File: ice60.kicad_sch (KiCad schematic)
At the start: 31 parts, among them J1 SWD, J2 JST SH 4-pin, SW0 SW_Push, U1 RP2040, U2 W25Q128JVS, U3 XC6206PxxxMR, U4 SRV05-4, Y1 12MHz

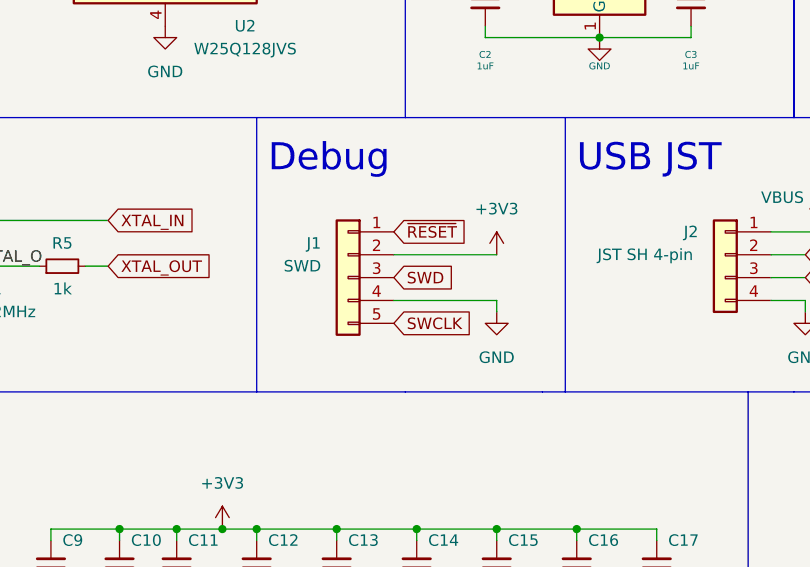
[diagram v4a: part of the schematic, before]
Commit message: swap bulk cap & reroute debug
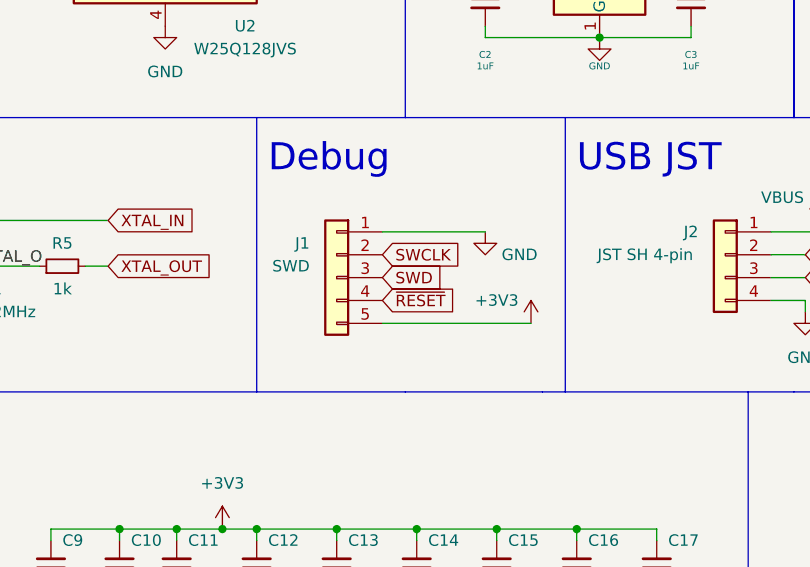
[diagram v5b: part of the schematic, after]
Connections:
- net +3V3: now also J1.5 (Pin_5); no longer J1.2 (Pin_2)
- net GND: now also J1.1 (Pin_1); no longer J1.4 (Pin_4)
- net SWCLK: now also J1.2 (Pin_2); no longer J1.5 (Pin_5)
- net ~{RESET}: now also J1.4 (Pin_4); no longer J1.1 (Pin_1)
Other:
- moved on the sheet: J1
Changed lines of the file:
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@@
     (stroke (width 0) (type default) (color 0 0 0 0))
   )
-  (wire (pts (xy 172.72 74.93) (xy 184.15 74.93))
+  (wire (pts (xy 171.45 67.31) (xy 182.88 67.31))
     (stroke (width 0) (type default) (color 0 0 0 0))
   )
@@
     (stroke (width 0) (type default) (color 0 0 0 0))
   )
-  (wire (pts (xy 184.15 76.2) (xy 184.15 74.93))
-    (stroke (width 0) (type default) (color 0 0 0 0))
-  )
-  (wire (pts (xy 172.72 69.85) (xy 184.15 69.85))
+  (wire (pts (xy 171.45 77.47) (xy 187.96 77.47))
     (stroke (width 0) (type default) (color 0 0 0 0))
   )
@@
     )
   )
-  (global_label "~{RESET}" (shape input) (at 172.72 67.31 0) (fields_autoplaced)
-    (effects (font (size 1.27 1.27)) (justify left))
-    (property "Intersheet References" "${INTERSHEET_REFS}" (id 0) (at 180.8783 67.2306 0)
+  (global_label "~{RESET}" (shape input) (at 171.45 74.93 0) (fields_autoplaced)
+    (effects (font (size 1.27 1.27)) (justify left))
+    (property "Intersheet References" "${INTERSHEET_REFS}" (id 0) (at 179.6083 74.8506 0)
       (effects (font (size 1.27 1.27)) (justify left) hide)
     )
@@
     )
   )
-  (global_label "SWCLK" (shape input) (at 172.72 77.47 0) (fields_autoplaced)
-    (effects (font (size 1.27 1.27)) (justify left))
-    (property "Intersheet References" "${INTERSHEET_REFS}" (id 0) (at 181.3621 77.3906 0)
+  (global_label "SWCLK" (shape input) (at 171.45 69.85 0) (fields_autoplaced)
+    (effects (font (size 1.27 1.27)) (justify left))
+    (property "Intersheet References" "${INTERSHEET_REFS}" (id 0) (at 180.0921 69.7706 0)
       (effects (font (size 1.27 1.27)) (justify left) hide)
     )
@@
     )
   )
-  (global_label "SWD" (shape input) (at 172.72 72.39 0) (fields_autoplaced)
-    (effects (font (size 1.27 1.27)) (justify left))
-    (property "Intersheet References" "${INTERSHEET_REFS}" (id 0) (at 179.0641 72.3106 0)
+  (global_label "SWD" (shape input) (at 171.45 72.39 0) (fields_autoplaced)
+    (effects (font (size 1.27 1.27)) (justify left))
+    (property "Intersheet References" "${INTERSHEET_REFS}" (id 0) (at 177.7941 72.3106 0)
       (effects (font (size 1.27 1.27)) (justify left) hide)
     )
@@
     (pin "2")
   )
-  (symbol (lib_id "power:+3V3") (at 184.15 69.85 0) (unit 1)
-    (in_bom yes) (on_board yes) (fields_autoplaced)
-    (property "Reference" "#PWR021" (id 0) (at 184.15 73.66 0)
-      (effects (font (size 1.27 1.27)) hide)
-    )
-    (property "Value" "+3V3" (id 1) (at 184.15 64.77 0))
-    (property "Footprint" "" (id 2) (at 184.15 69.85 0)
-      (effects (font (size 1.27 1.27)) hide)
-    )
-    (property "Datasheet" "" (id 3) (at 184.15 69.85 0)
+  (symbol (lib_id "power:+3V3") (at 187.96 77.47 0) (unit 1)
+    (in_bom yes) (on_board yes)
+    (property "Reference" "#PWR021" (id 0) (at 187.96 81.28 0)
+      (effects (font (size 1.27 1.27)) hide)
+    )
+    (property "Value" "+3V3" (id 1) (at 184.15 74.93 0))
+    (property "Footprint" "" (id 2) (at 187.96 77.47 0)
+      (effects (font (size 1.27 1.27)) hide)
+    )
+    (property "Datasheet" "" (id 3) (at 187.96 77.47 0)
       (effects (font (size 1.27 1.27)) hide)
     )
@@
     (pin "2")
   )
-  (symbol (lib_id "Connector_Generic:Conn_01x05") (at 167.64 72.39 0) (mirror y) (unit 1)
+  (symbol (lib_id "Connector_Generic:Conn_01x05") (at 166.37 72.39 0) (mirror y) (unit 1)
     (in_bom no) (on_board yes)
-    (property "Reference" "J1" (id 0) (at 163.83 68.58 0))
-    (property "Value" "SWD" (id 1) (at 162.56 71.12 0))
-    (property "Footprint" "Connector_PinSocket_2.54mm:PinSocket_1x05_P2.54mm_Vertical" (id 2) (at 167.64 72.39 0)
-      (effects (font (size 1.27 1.27)) hide)
-    )
-    (property "Datasheet" "~" (id 3) (at 167.64 72.39 0)
+    (property "Reference" "J1" (id 0) (at 162.56 68.58 0))
+    (property "Value" "SWD" (id 1) (at 161.29 71.12 0))
+    (property "Footprint" "Connector_PinSocket_2.54mm:PinSocket_1x05_P2.54mm_Vertical" (id 2) (at 166.37 72.39 0)
+      (effects (font (size 1.27 1.27)) hide)
+    )
+    (property "Datasheet" "~" (id 3) (at 166.37 72.39 0)
       (effects (font (size 1.27 1.27)) hide)
     )
@@
     (pin "1")
   )
-  (symbol (lib_id "power:GND") (at 184.15 76.2 0) (unit 1)
-    (in_bom yes) (on_board yes) (fields_autoplaced)
-    (property "Reference" "#PWR022" (id 0) (at 184.15 82.55 0)
-      (effects (font (size 1.27 1.27)) hide)
-    )
-    (property "Value" "GND" (id 1) (at 184.15 81.28 0))
-    (property "Footprint" "" (id 2) (at 184.15 76.2 0)
-      (effects (font (size 1.27 1.27)) hide)
-    )
-    (property "Datasheet" "" (id 3) (at 184.15 76.2 0)
-      (effects (font (size 1.27 1.27)) hide)
-    )
+  (symbol (lib_id "power:GND") (at 182.88 67.31 0) (unit 1)
+    (in_bom yes) (on_board yes)
+    (property "Reference" "#PWR022" (id 0) (at 182.88 73.66 0)
+      (effects (font (size 1.27 1.27)) hide)
+    )
+    (property "Value" "GND" (id 1) (at 186.69 69.85 0))
+    (property "Footprint" "" (id 2) (at 182.88 67.31 0)
+      (effects (font (size 1.27 1.27)) hide)
+    )
+    (property "Datasheet" "" (id 3) (at 182.88 67.31 0)
+      (effects (font (size 1.27 1.27)) hide)
+    )

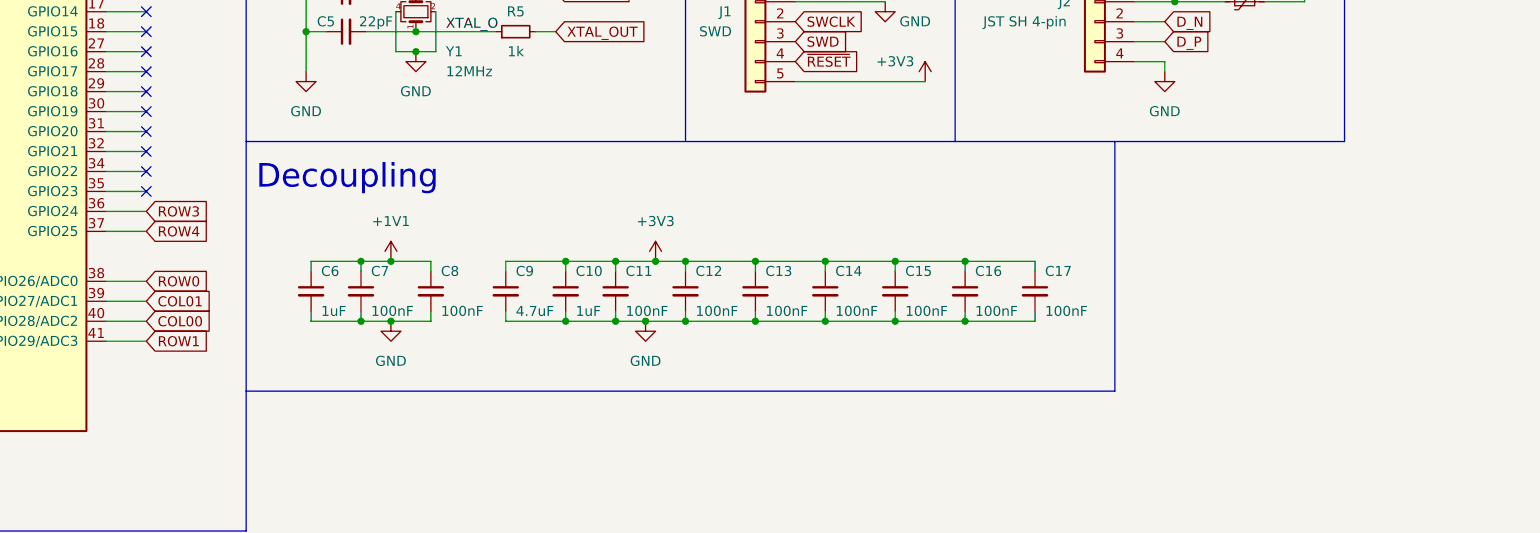
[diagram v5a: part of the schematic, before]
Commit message: add capslock in-switch LED indicator
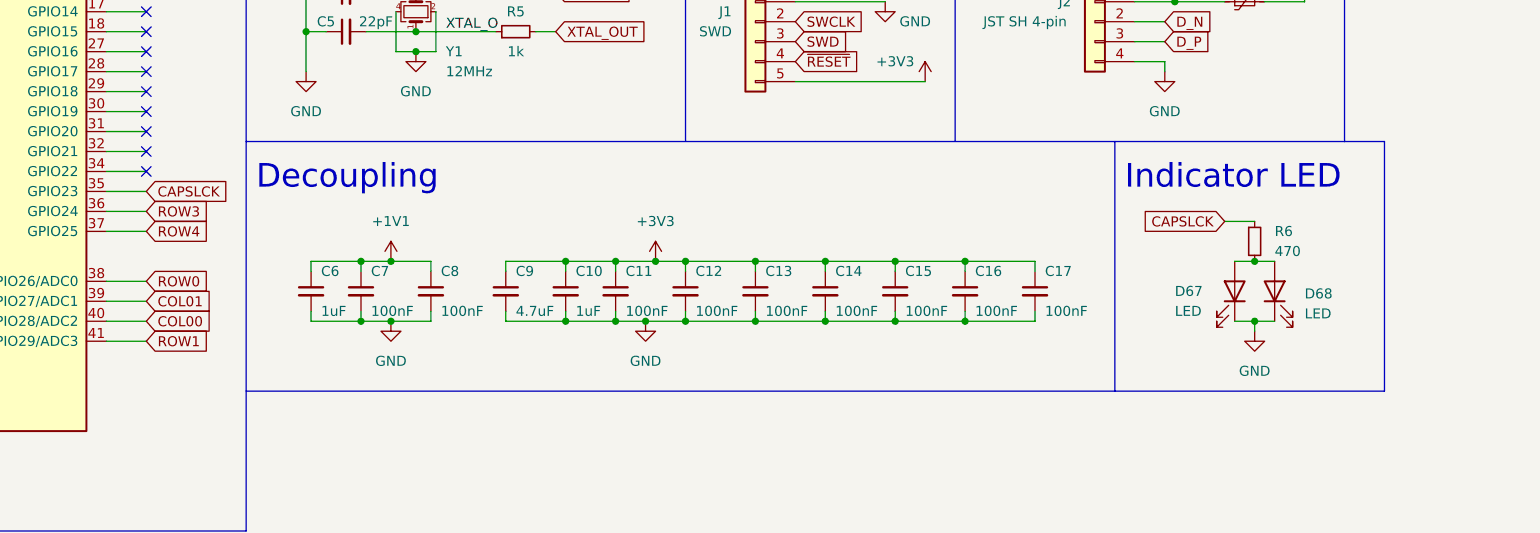
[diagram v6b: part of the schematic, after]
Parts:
- added D67: LED, marbastlib-mx:LED_MX_3mm, symbol Device:LED
- added D68: LED, marbastlib-mx:LED_MX_3mm-FLIPPED, symbol Device:LED
- added R6: 470, Resistor_SMD:R_0402_1005Metric, symbol Device:R_Small
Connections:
- net GND: now also D67.1 (K), D68.1 (K)
- net CAPSLCK: now reaches U1.35 (GPIO23)
- net CAPSLCK: now also R6.1
- new net: D67.2 (A), D68.2 (A), R6.2
- no-connect marks 13 -> 12
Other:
- note added: "Indicator LED"
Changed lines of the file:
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@@
     (comment 4 "60% Soldered PCB with JST Powered by RP2040")
   )
+  (junction (at 229.87 100.33) (diameter 0) (color 0 0 0 0)
+  )
   (junction (at 123.19 73.66) (diameter 0) (color 0 0 0 0)
   )
@@
   )
   (junction (at 109.22 71.12) (diameter 0) (color 0 0 0 0)
+  )
+  (junction (at 229.87 107.95) (diameter 0) (color 0 0 0 0)
   )
   (junction (at 147.32 22.86) (diameter 0) (color 0 0 0 0)
@@
   (no_connect (at 88.9 86.36))
   (no_connect (at 227.33 38.1))
-  (no_connect (at 88.9 91.44))
   (no_connect (at 88.9 83.82))
   (no_connect (at 88.9 73.66))
   (no_connect (at 88.9 71.12))
   (no_connect (at 88.9 76.2))
+  (wire (pts (xy 229.87 107.95) (xy 232.41 107.95))
+    (stroke (width 0) (type default) (color 0 0 0 0))
+  )
   (polyline (pts (xy 15.24 15.24) (xy 15.24 134.62))
     (stroke (width 0) (type default) (color 0 0 0 0))
@@
     (stroke (width 0) (type default) (color 0 0 0 0))
   )
+  (wire (pts (xy 229.87 100.33) (xy 227.33 100.33))
+    (stroke (width 0) (type default) (color 0 0 0 0))
+  )
   (wire (pts (xy 203.2 38.1) (xy 205.74 38.1))
     (stroke (width 0) (type solid) (color 0 0 0 0))
@@
     (stroke (width 0) (type default) (color 0 0 0 0))
   )
+  (wire (pts (xy 226.06 95.25) (xy 229.87 95.25))
+    (stroke (width 0) (type default) (color 0 0 0 0))
+  )
   (wire (pts (xy 83.82 71.12) (xy 88.9 71.12))
     (stroke (width 0) (type default) (color 0 0 0 0))
@@
   )
   (wire (pts (xy 88.9 88.9) (xy 83.82 88.9))
+    (stroke (width 0) (type default) (color 0 0 0 0))
+  )
+  (polyline (pts (xy 246.38 116.84) (xy 246.38 85.09))
     (stroke (width 0) (type default) (color 0 0 0 0))
   )
@@
     (stroke (width 0) (type default) (color 0 0 0 0))
   )
+  (polyline (pts (xy 212.09 116.84) (xy 246.38 116.84))
+    (stroke (width 0) (type default) (color 0 0 0 0))
+  )
   (polyline (pts (xy 101.6 15.24) (xy 173.99 15.24))
     (stroke (width 0) (type default) (color 0 0 0 0))
@@
     (stroke (width 0) (type default) (color 0 0 0 0))
   )
+  (wire (pts (xy 227.33 107.95) (xy 229.87 107.95))
+    (stroke (width 0) (type default) (color 0 0 0 0))
+  )
   (wire (pts (xy 134.62 100.33) (xy 142.24 100.33))
     (stroke (width 0) (type default) (color 0 0 0 0))
@@
   )
   (wire (pts (xy 201.93 100.33) (xy 201.93 101.6))
+    (stroke (width 0) (type default) (color 0 0 0 0))
+  )
+  (polyline (pts (xy 241.3 85.09) (xy 246.38 85.09))
     (stroke (width 0) (type default) (color 0 0 0 0))
   )
@@
     (stroke (width 0) (type default) (color 0 0 0 0))
   )
+  (wire (pts (xy 229.87 100.33) (xy 232.41 100.33))
+    (stroke (width 0) (type default) (color 0 0 0 0))
+  )
   (polyline (pts (xy 241.3 54.61) (xy 241.3 85.09))
     (stroke (width 0) (type default) (color 0 0 0 0))
@@
     (stroke (width 0) (type default) (color 0 0 0 0))
   )
+  (wire (pts (xy 229.87 107.95) (xy 229.87 109.22))
+    (stroke (width 0) (type default) (color 0 0 0 0))
+  )
   (wire (pts (xy 109.855 107.95) (xy 116.205 107.95))
     (stroke (width 0) (type default) (color 0 0 0 0))
   )
   (text "Crystal" (at 102.87 60.96 0)
+    (effects (font (size 3 3)) (justify left bottom))
+  )
+  (text "Indicator LED\n" (at 213.36 91.44 0)
     (effects (font (size 3 3)) (justify left bottom))
   )
@@
     )
   )
+  (global_label "CAPSLCK" (shape input) (at 226.06 95.25 180) (fields_autoplaced)
+    (effects (font (size 1.27 1.27)) (justify right))
+    (property "Intersheet References" "${INTERSHEET_REFS}" (id 0) (at 215.2407 95.1706 0)
+      (effects (font (size 1.27 1.27)) (justify right) hide)
+    )
+  )
   (global_label "CS" (shape input) (at 133.35 31.75 90) (fields_autoplaced)
     (effects (font (size 1.27 1.27)) (justify left))
@@
     (effects (font (size 1.27 1.27)) (justify left))
     (property "Intersheet References" "${INTERSHEET_REFS}" (id 0) (at 150.5798 65.9606 0)
+      (effects (font (size 1.27 1.27)) (justify left) hide)
+    )
+  )
+  (global_label "CAPSLCK" (shape input) (at 88.9 91.44 0) (fields_autoplaced)
+    (effects (font (size 1.27 1.27)) (justify left))
+    (property "Intersheet References" "${INTERSHEET_REFS}" (id 0) (at 99.7193 91.5194 0)
       (effects (font (size 1.27 1.27)) (justify left) hide)
     )
@@
     )
     (pin "1")
+  )
+  (symbol (lib_id "Device:LED") (at 227.33 104.14 270) (mirror x) (unit 1)
+    (in_bom yes) (on_board yes)
+    (property "Reference" "D67" (id 0) (at 219.71 104.14 90)
+      (effects (font (size 1.27 1.27)) (justify left))
+    )
+    (property "Value" "LED" (id 1) (at 219.71 106.68 90)
+      (effects (font (size 1.27 1.27)) (justify left))
+    )
+    (property "Footprint" "marbastlib-mx:LED_MX_3mm" (id 2) (at 227.33 104.14 0)
+      (effects (font (size 1.27 1.27)) hide)
+    )
+    (property "Datasheet" "~" (id 3) (at 227.33 104.14 0)
+      (effects (font (size 1.27 1.27)) hide)
+    )
+    (pin "1")
+    (pin "2")
   )
   (symbol (lib_id "power:GND") (at 106.045 31.75 0) (unit 1)
@@
     (pin "2")
   )
+  (symbol (lib_id "power:GND") (at 229.87 109.22 0) (unit 1)
+    (in_bom yes) (on_board yes) (fields_autoplaced)
+    (property "Reference" "#PWR0105" (id 0) (at 229.87 115.57 0)
+      (effects (font (size 1.27 1.27)) hide)
+    )
+    (property "Value" "GND" (id 1) (at 229.87 114.3 0))
+    (property "Footprint" "" (id 2) (at 229.87 109.22 0)
+      (effects (font (size 1.27 1.27)) hide)
+    )
+    (property "Datasheet" "" (id 3) (at 229.87 109.22 0)
+      (effects (font (size 1.27 1.27)) hide)
+    )
+    (pin "1")
+  )
   (symbol (lib_id "Regulator_Linear:XC6206PxxxMR") (at 195.58 38.1 0) (unit 1)
     (in_bom yes) (on_board yes) (fields_autoplaced)
@@
     (pin "1")
   )
+  (symbol (lib_id "Device:LED") (at 232.41 104.14 90) (unit 1)
+    (in_bom yes) (on_board yes) (fields_autoplaced)
+    (property "Reference" "D68" (id 0) (at 236.22 104.4574 90)
+      (effects (font (size 1.27 1.27)) (justify right))
+    )
+    (property "Value" "LED" (id 1) (at 236.22 106.9974 90)
+      (effects (font (size 1.27 1.27)) (justify right))
+    )
+    (property "Footprint" "marbastlib-mx:LED_MX_3mm-FLIPPED" (id 2) (at 232.41 104.14 0)
+      (effects (font (size 1.27 1.27)) hide)
+    )
+    (property "Datasheet" "~" (id 3) (at 232.41 104.14 0)
+      (effects (font (size 1.27 1.27)) hide)
+    )
+    (pin "1")
+    (pin "2")
+  )
   (symbol (lib_id "power:GND") (at 240.03 49.53 0) (mirror y) (unit 1)
     (in_bom yes) (on_board yes)
@@
     )
     (pin "1")
+  )
+  (symbol (lib_id "Device:R_Small") (at 229.87 97.79 0) (unit 1)
+    (in_bom yes) (on_board yes) (fields_autoplaced)
+    (property "Reference" "R6" (id 0) (at 232.41 96.5199 0)
+      (effects (font (size 1.27 1.27)) (justify left))
+    )
+    (property "Value" "470" (id 1) (at 232.41 99.0599 0)
+      (effects (font (size 1.27 1.27)) (justify left))
+    )
+    (property "Footprint" "Resistor_SMD:R_0402_1005Metric" (id 2) (at 229.87 97.79 0)
+      (effects (font (size 1.27 1.27)) hide)
+    )
+    (property "Datasheet" "~" (id 3) (at 229.87 97.79 0)
+      (effects (font (size 1.27 1.27)) hide)
+    )
+    (pin "1")
+    (pin "2")
   )
   (symbol (lib_id "Device:Polyfuse_Small") (at 228.6 67.31 90) (unit 1)
@@
       (reference "#PWR0104") (unit 1) (value "+5V") (footprint "")
     )
+    (path "/9e7662d2-273c-4d25-8c91-9b990718ac1e"
+      (reference "#PWR0105") (unit 1) (value "GND") (footprint "")
+    )
     (path "/56077389-3dc3-4dac-9d26-70524308becc"
       (reference "C1") (unit 1) (value "100nF") (footprint "Capacitor_SMD:C_0402_1005Metric")
@@
       (reference "D66") (unit 1) (value "D_Small") (footprint "Diode_SMD:D_SOD-123")
     )
+    (path "/22ee8c76-6751-4dce-b25d-cb8e42cd2337"
+      (reference "D67") (unit 1) (value "LED") (footprint "marbastlib-mx:LED_MX_3mm")
+    )
+    (path "/f1020f49-8bd3-48f1-9c97-8a989f4cc3e0"
+      (reference "D68") (unit 1) (value "LED") (footprint "marbastlib-mx:LED_MX_3mm-FLIPPED")
+    )
     (path "/f97e6b76-28e1-4562-9d3c-964873c21128"
       (reference "F1") (unit 1) (value "500mA") (footprint "Fuse:Fuse_1206_3216Metric")
@@
       (reference "R5") (unit 1) (value "1k") (footprint "Resistor_SMD:R_0402_1005Metric")
     )
+    (path "/f4dc9ca1-a46b-480b-8045-0daec62f2914"
+      (reference "R6") (unit 1) (value "470") (footprint "Resistor_SMD:R_0402_1005Metric")
+    )
     (path "/99b63952-0e82-445f-a871-af9a28c1c443"
